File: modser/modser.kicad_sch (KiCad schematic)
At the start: 3 parts, among them IC1 AS5600-ASOT, U1 DRV8313PWPR, U2 XIAO-RP2040-DIP

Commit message: Schematic draft complete!
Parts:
- added C1, C4, C6, C8: 100 nF, symbol Device:C
- added C10, C11: 22 uF, symbol Device:C
- added C2: 100 uF Polarized, symbol Device:C_Polarized
- added C3: 0.47 uF, symbol Device:C
- added C5: 10 nF, symbol Device:C
- added C7: 10 uF, symbol Device:C
- added C9: 100 pF, symbol Device:C
- added J1: Conn_01x03_Socket, symbol Connector:Conn_01x03_Socket
- added L1: 2.2 uH, symbol Device:L
- added R1: 10 kOhm, symbol Device:R
- added R2: 30.9 kOhm, symbol Device:R
- added R3: 62 kOhm, symbol Device:R
- added U3: AP63203WU-7, LIB_AP63203WU-7:AP63203WU7, symbol 2025-08-06_01-37-09:AP63203WU-7
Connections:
- net +3.3V: now reaches IC1.1 (VDD5V)
- net +3.3V: now also IC1.2 (VDD3V3), U1.15 (V3P3), U2.12 (3V3), C10.1, C11.1, C3.2, C6.1, C9.1, L1.2, R1.2, R2.1
- net GND: now reaches IC1.4 (GND)
- net GND: now also IC1.8 (DIR), U1.10 (PGND3), U1.12 (COMPP), U1.13 (COMPN), U1.14 (GND), U1.19 (~{COMPO}), U1.20 (GND__1), U1.21 (NC), U1.28 (GND__2), U1.6 (PGND1), U1.7 (PGND2), U2.13 (GND), C10.2, C11.2, C2.2, C3.1, C4.2, C6.2, C7.2, R3.2, U3.4 (GND)
- net at IC1.6 (SDA): now also U2.5 (GPIO6/SDA)
- net at IC1.7 (SCL): now also U2.6 (GPIO7/SCL)
- net at U2.1 (GPIO26/ADC0/A0): now also U1.27 (IN1)
- net at U2.2 (GPIO27/ADC1/A1): now also U1.25 (IN2)
- net at U2.3 (GPIO28/ADC2/A2): now also U1.23 (IN3)
- net Enable: now reaches U2.4 (GPIO29/ADC3/A3)
- net Enable: now also U1.22 (EN3), U1.24 (EN2), U1.26 (EN1)
- net at U1.1 (CPL): now also C5.1
- net VCC: now reaches U1.11 (VM__1)
- net VCC: now also U1.4 (VM), C1.1, C2.1, C4.1, C7.1, U3.2 (EN), U3.3 (VIN)
- net at U1.18 (~{FAULT}): now also R1.1
- net at U1.2 (CPH): now also C5.2
- net at U1.3 (VCP): now also C1.2
- net at U1.5 (OUT1): now also J1.1 (Pin_1)
- net at U1.8 (OUT2): now also J1.2 (Pin_2)
- net at U1.9 (OUT3): now also J1.3 (Pin_3)
- new net: C8.2, L1.1, U3.5 (SW)
- new net: C8.1, U3.6 (BST)
- new net RegFB: C9.2, R2.2, R3.1, U3.1 (FB)
- no-connect marks 0 -> 11
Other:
- moved on the sheet: IC1, U1, U2

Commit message: Created general outline, speced passives
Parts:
- added J3: Conn_01x02_Socket, Connector_PinHeader_2.54mm:PinHeader_1x02_P2.54mm_Vertical, symbol Connector:Conn_01x02_Socket
- C1, C3, C4, C5, C6, C8, C9: footprint (none) -> Capacitor_SMD:C_0603_1608Metric_Pad1.08x0.95mm_HandSolder
- C10, C11, C7: footprint (none) -> Capacitor_SMD:C_1206_3216Metric
- J1: footprint (none) -> Connector_PinHeader_2.54mm:PinHeader_1x03_P2.54mm_Vertical
- R1, R2, R3: footprint (none) -> Resistor_SMD:R_0603_1608Metric_Pad0.98x0.95mm_HandSolder
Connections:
- net GND: now also J3.2 (Pin_2)
- net VCC: now also J3.1 (Pin_1)
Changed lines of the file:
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@@
 			)
 		)
-		(property "Footprint" ""
+		(property "Footprint" "Resistor_SMD:R_0603_1608Metric_Pad0.98x0.95mm_HandSolder"
 			(at 179.832 134.62 90)
 			(effects
@@
 	)
 	(symbol
+		(lib_id "Connector:Conn_01x02_Socket")
+		(at 214.63 69.85 0)
+		(unit 1)
+		(exclude_from_sim no)
+		(in_bom yes)
+		(on_board yes)
+		(dnp no)
+		(fields_autoplaced yes)
+		(property "Reference" "J3"
+			(at 215.9 69.8499 0)
+			(effects
+				(font
+					(size 1.27 1.27)
+				)
+				(justify left)
+			)
+		)
+		(property "Value" "Conn_01x02_Socket"
+			(at 215.9 72.3899 0)
+			(effects
+				(font
+					(size 1.27 1.27)
+				)
+				(justify left)
+			)
+		)
+		(property "Footprint" "Connector_PinHeader_2.54mm:PinHeader_1x02_P2.54mm_Vertical"
+			(at 214.63 69.85 0)
+			(effects
+				(font
+					(size 1.27 1.27)
+				)
+				(hide yes)
+			)
+		)
+		(property "Datasheet" "~"
+			(at 214.63 69.85 0)
+			(effects
+				(font
+					(size 1.27 1.27)
+				)
+				(hide yes)
+			)
+		)
+		(property "Description" "Generic connector, single row, 01x02, script generated"
+			(at 214.63 69.85 0)
+			(effects
+				(font
+					(size 1.27 1.27)
+				)
+				(hide yes)
+			)
+		)
+		(pin "2"
+		)
+		(pin "1"
+		)
+		(instances
+			(project ""
+				(path "/01c17a33-9bbc-4187-99d4-a03f0d327a97"
+					(reference "J3")
+					(unit 1)
+				)
+			)
+		)
+	)
+	(symbol
 		(lib_id "power:+3.3V")
 		(at 210.82 123.19 270)
@@
 	)
 	(symbol
+		(lib_id "power:GND")
+		(at 209.55 72.39 270)
+		(unit 1)
+		(exclude_from_sim no)
+		(in_bom yes)
+		(on_board yes)
+		(dnp no)
+		(fields_autoplaced yes)
+		(property "Reference" "#PWR014"
+			(at 203.2 72.39 0)
+			(effects
+				(font
+					(size 1.27 1.27)
+				)
+				(hide yes)
+			)
+		)
+		(property "Value" "GND"
+			(at 205.74 72.3899 90)
+			(effects
+				(font
+					(size 1.27 1.27)
+				)
+				(justify right)
+			)
+		)
+		(property "Footprint" ""
+			(at 209.55 72.39 0)
+			(effects
+				(font
+					(size 1.27 1.27)
+				)
+				(hide yes)
+			)
+		)
+		(property "Datasheet" ""
+			(at 209.55 72.39 0)
+			(effects
+				(font
+					(size 1.27 1.27)
+				)
+				(hide yes)
+			)
+		)
+		(property "Description" "Power symbol creates a global label with name \"GND\" , ground"
+			(at 209.55 72.39 0)
+			(effects
+				(font
+					(size 1.27 1.27)
+				)
+				(hide yes)
+			)
+		)
+		(pin "1"
+		)
+		(instances
+			(project "modser"
+				(path "/01c17a33-9bbc-4187-99d4-a03f0d327a97"
+					(reference "#PWR014")
+					(unit 1)
+				)
+			)
+		)
+	)
+	(symbol
 		(lib_id "Device:L")
 		(at 166.37 123.19 90)
@@
 			)
 		)
-		(property "Footprint" ""
+		(property "Footprint" "Capacitor_SMD:C_0603_1608Metric_Pad1.08x0.95mm_HandSolder"
 			(at 159.0548 58.42 0)
 			(effects
@@
 			)
 		)
-		(property "Footprint" ""
+		(property "Footprint" "Capacitor_SMD:C_0603_1608Metric_Pad1.08x0.95mm_HandSolder"
 			(at 161.29 114.6048 0)
 			(effects
@@
 			)
 		)
-		(property "Footprint" ""
+		(property "Footprint" "Resistor_SMD:R_0603_1608Metric_Pad0.98x0.95mm_HandSolder"
 			(at 154.94 60.198 90)
 			(effects
@@
 			)
 		)
-		(property "Footprint" ""
+		(property "Footprint" "Capacitor_SMD:C_0603_1608Metric_Pad1.08x0.95mm_HandSolder"
 			(at 171.1452 130.81 0)
 			(effects
@@
 			)
 		)
-		(property "Footprint" ""
+		(property "Footprint" "Capacitor_SMD:C_0603_1608Metric_Pad1.08x0.95mm_HandSolder"
 			(at 152.0952 45.72 0)
 			(effects
@@
 			)
 		)
-		(property "Footprint" ""
+		(property "Footprint" "Capacitor_SMD:C_1206_3216Metric"
 			(at 200.3552 134.62 0)
 			(effects
@@
 			)
 		)
-		(property "Footprint" ""
+		(property "Footprint" "Capacitor_SMD:C_0603_1608Metric_Pad1.08x0.95mm_HandSolder"
 			(at 40.3352 135.89 0)
 			(effects
@@
 	)
 	(symbol
+		(lib_id "power:VCC")
+		(at 209.55 69.85 90)
+		(unit 1)
+		(exclude_from_sim no)
+		(in_bom yes)
+		(on_board yes)
+		(dnp no)
+		(fields_autoplaced yes)
+		(property "Reference" "#PWR013"
+			(at 213.36 69.85 0)
+			(effects
+				(font
+					(size 1.27 1.27)
+				)
+				(hide yes)
+			)
+		)
+		(property "Value" "VCC"
+			(at 205.74 69.8499 90)
+			(effects
+				(font
+					(size 1.27 1.27)
+				)
+				(justify left)
+			)
+		)
+		(property "Footprint" ""
+			(at 209.55 69.85 0)
+			(effects
+				(font
+					(size 1.27 1.27)
+				)
+				(hide yes)
+			)
+		)
+		(property "Datasheet" ""
+			(at 209.55 69.85 0)
+			(effects
+				(font
+					(size 1.27 1.27)
+				)
+				(hide yes)
+			)
+		)
+		(property "Description" "Power symbol creates a global label with name \"VCC\""
+			(at 209.55 69.85 0)
+			(effects
+				(font
+					(size 1.27 1.27)
+				)
+				(hide yes)
+			)
+		)
+		(pin "1"
+		)
+		(instances
+			(project "modser"
+				(path "/01c17a33-9bbc-4187-99d4-a03f0d327a97"
+					(reference "#PWR013")
+					(unit 1)
+				)
+			)
+		)
+	)
+	(symbol
 		(lib_id "Device:R")
 		(at 181.61 127 0)
@@
 			)
 		)
-		(property "Footprint" ""
+		(property "Footprint" "Resistor_SMD:R_0603_1608Metric_Pad0.98x0.95mm_HandSolder"
 			(at 179.832 127 90)
 			(effects
@@
 			)
 		)
-		(property "Footprint" ""
+		(property "Footprint" "Capacitor_SMD:C_0603_1608Metric_Pad1.08x0.95mm_HandSolder"
 			(at 188.9252 43.18 0)
 			(effects
@@
 			)
 		)
-		(property "Footprint" ""
+		(property "Footprint" "Capacitor_SMD:C_0603_1608Metric_Pad1.08x0.95mm_HandSolder"
 			(at 153.3652 27.94 0)
 			(effects
@@
 			)
 		)
-		(property "Footprint" ""
+		(property "Footprint" "Capacitor_SMD:C_1206_3216Metric"
 			(at 211.7852 134.62 0)
 			(effects
@@
 			)
 		)
-		(property "Footprint" ""
+		(property "Footprint" "Capacitor_SMD:C_1206_3216Metric"
 			(at 113.9952 137.16 0)
 			(effects
@@
 			)
 		)
-		(property "Footprint" ""
+		(property "Footprint" "Connector_PinHeader_2.54mm:PinHeader_1x03_P2.54mm_Vertical"
 			(at 196.85 50.8 0)
 			(effects

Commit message: Finished layout, working on getting all 3d models added
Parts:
- C2: footprint (none) -> LIB_UCL1E101MCL1GS:CAPAE660X800N
- L1: footprint (none) -> LQM2MPN2R2NG0L:INDC2016X100N
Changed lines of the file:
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@@
 			)
 		)
-		(property "Footprint" ""
+		(property "Footprint" "LQM2MPN2R2NG0L:INDC2016X100N"
 			(at 166.37 123.19 0)
 			(effects
@@
 			)
 		)
-		(property "Footprint" ""
+		(property "Footprint" "LIB_UCL1E101MCL1GS:CAPAE660X800N"
 			(at 166.0652 43.18 0)
 			(effects

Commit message: Fixed issue with design around power regulator
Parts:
- removed C9: 100 pF, Capacitor_SMD:C_0603_1608Metric_Pad1.08x0.95mm_HandSolder, symbol Device:C
- removed R2: 30.9 kOhm, Resistor_SMD:R_0603_1608Metric_Pad0.98x0.95mm_HandSolder, symbol Device:R
- removed R3: 62 kOhm, Resistor_SMD:R_0603_1608Metric_Pad0.98x0.95mm_HandSolder, symbol Device:R
- L1: value 2.2 uH -> 3.9 uH
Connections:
- net RegFB is gone; now on net +3.3V: U3.1 (FB)

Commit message: Fixed issue where reset and sleep lines were never pulled high as required
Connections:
- net Enable: now also U1.16 (~{RESET}), U1.17 (~{SLEEP})
- no-connect marks 11 -> 9
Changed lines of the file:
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@@
+	)
+	(junction
+		(at 107.95 43.18)
+		(diameter 0)
+		(color 0 0 0 0)
 	)
 	(junction
@@
 	)
 	(junction
+		(at 107.95 38.1)
+		(diameter 0)
+		(color 0 0 0 0)
+	)
+	(junction
 		(at 199.39 138.43)
 		(diameter 0)
@@
 		(diameter 0)
 		(color 0 0 0 0)
-	)
-	(no_connect
-		(at 111.76 35.56)
 	)
 	(no_connect
@@
 	)
 	(no_connect
-		(at 111.76 38.1)
-	)
-	(no_connect
 		(at 80.01 97.79)
 	)
@@
 	(wire
 		(pts
+			(xy 107.95 43.18) (xy 107.95 38.1)
+		)
+		(stroke
+			(width 0)
+			(type default)
+		)
+	)
+	(wire
+		(pts
 			(xy 147.32 81.28) (xy 165.1 81.28)
 		)
@@
 	(wire
 		(pts
+			(xy 107.95 38.1) (xy 107.95 35.56)
+		)
+		(stroke
+			(width 0)
+			(type default)
+		)
+	)
+	(wire
+		(pts
 			(xy 39.37 90.17) (xy 44.45 90.17)
 		)
@@
 	(wire
 		(pts
+			(xy 107.95 35.56) (xy 111.76 35.56)
+		)
+		(stroke
+			(width 0)
+			(type default)
+		)
+	)
+	(wire
+		(pts
 			(xy 165.1 43.18) (xy 165.1 66.04)
 		)
@@
 		)
 		(stroke
+			(width 0)
+			(type default)
+		)
+	)
+	(wire
+		(pts
+			(xy 107.95 38.1) (xy 111.76 38.1)
+		)
+		(stroke

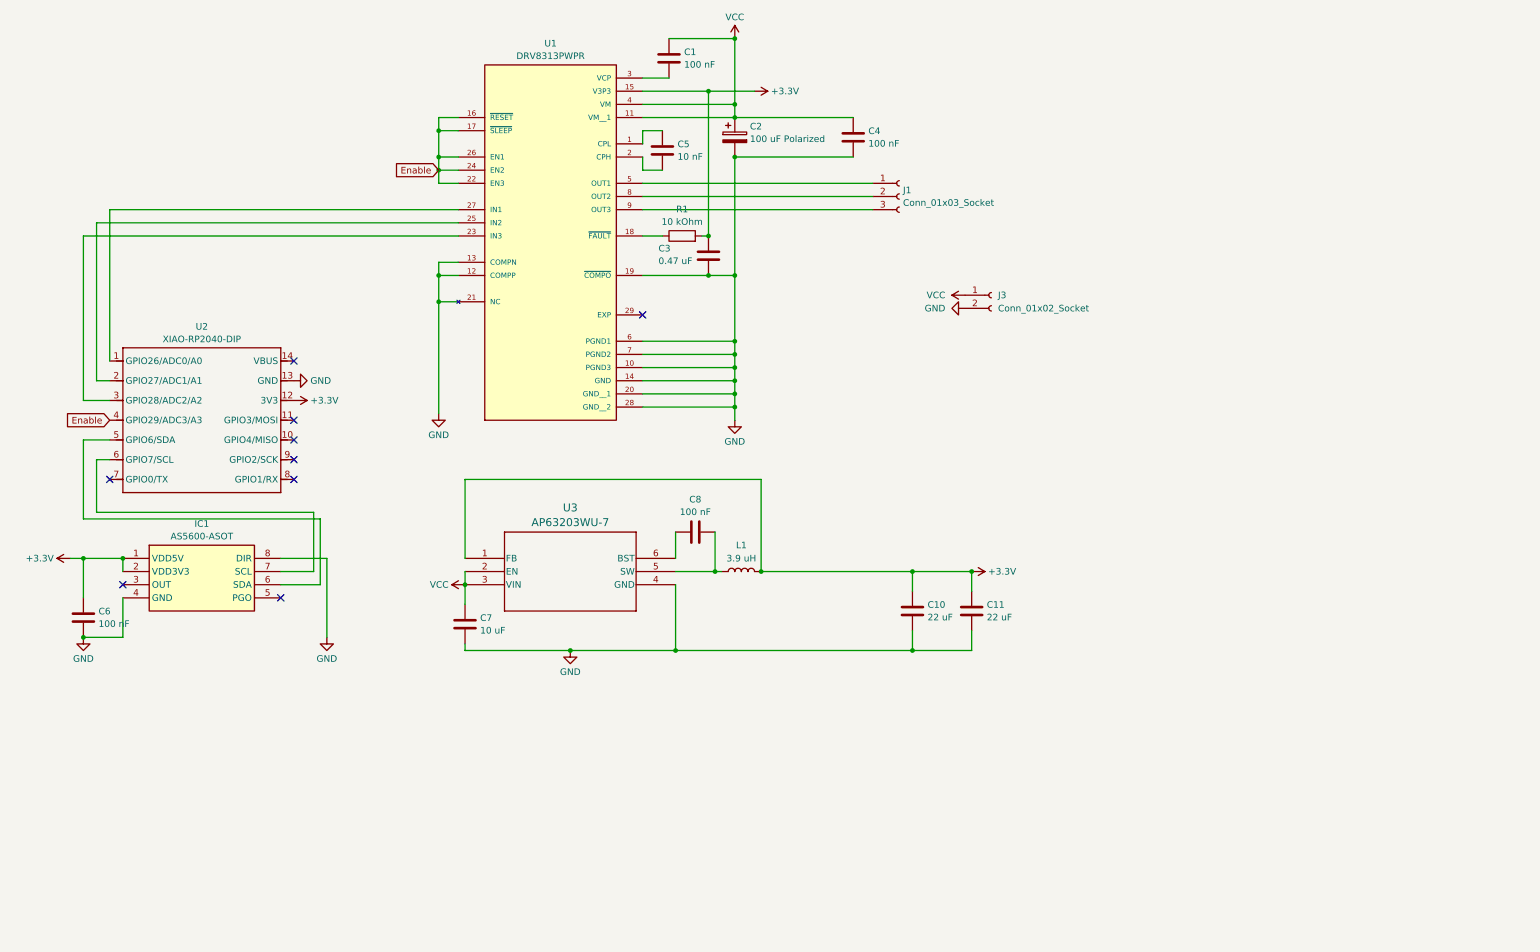
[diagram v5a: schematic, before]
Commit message: Updated schematic with can bus lines
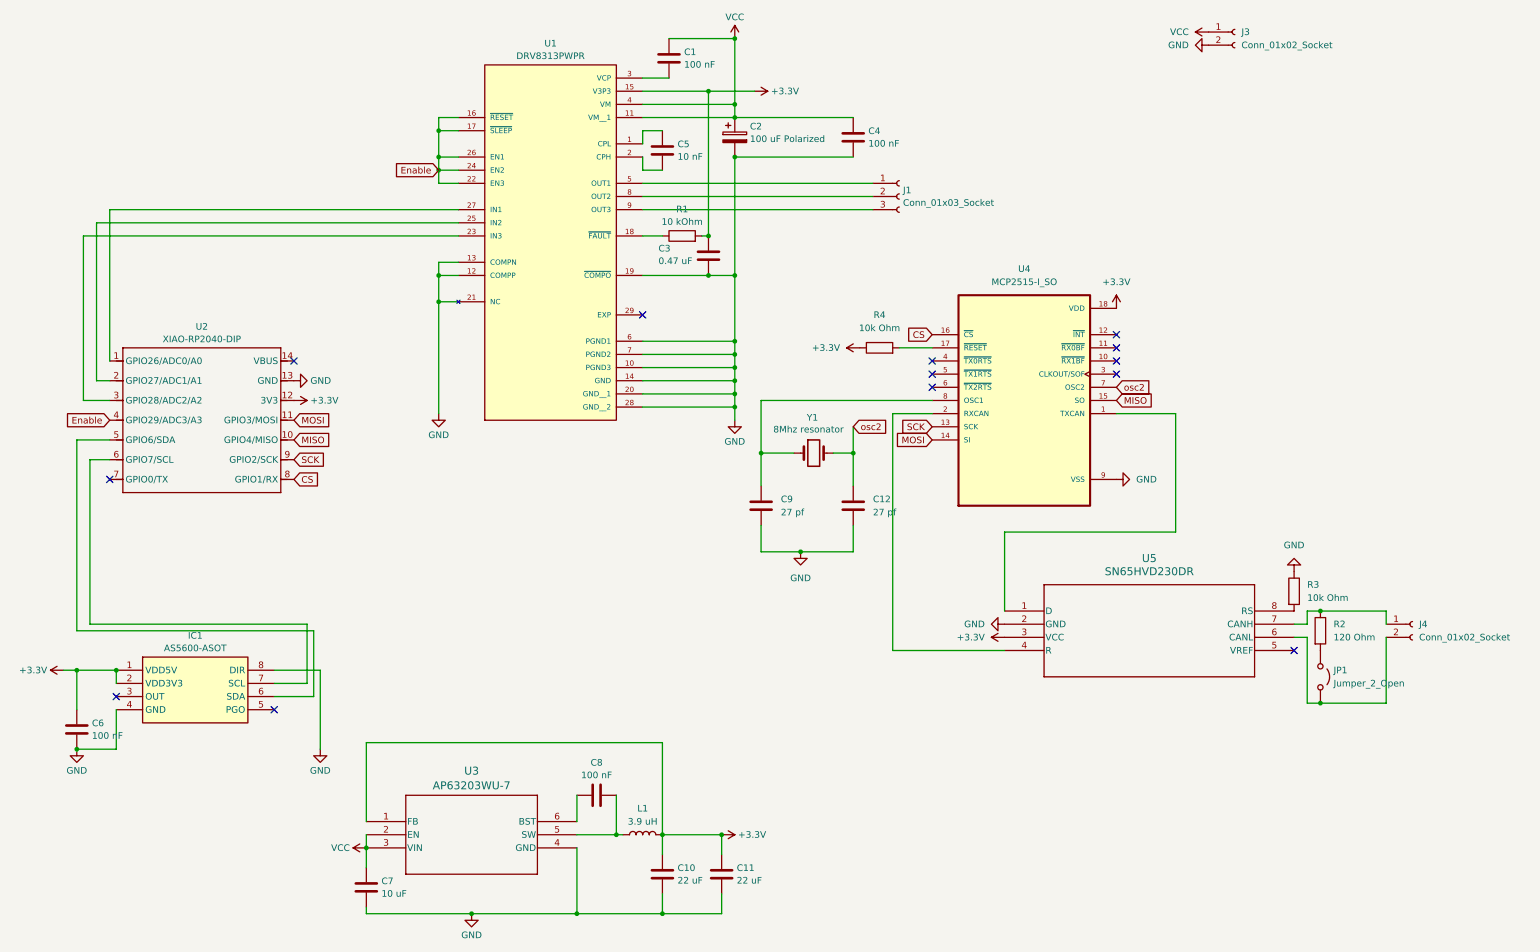
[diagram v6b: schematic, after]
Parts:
- added C12, C9: 27 pf, symbol Device:C
- added J4: Conn_01x02_Socket, symbol Connector:Conn_01x02_Socket
- added JP1: Jumper_2_Open, symbol Jumper:Jumper_2_Open
- added R2: 120 Ohm, symbol Device:R
- added R3, R4: 10k Ohm, symbol Device:R
- added U4: MCP2515-I_SO, MCP2515-I_SO:SOIC127P1030X265-18N, symbol MCP2515-I_SO:MCP2515-I_SO
- added U5: SN65HVD230DR, D8, symbol 2025-11-09_01-42-57:SN65HVD230DR
- added Y1: 8Mhz resonator, symbol Device:Crystal
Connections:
- net +3.3V: now also R4.1, U4.18 (VDD), U5.3 (VCC)
- net GND: now also C12.2, C9.2, R3.1, U4.9 (VSS), U5.2 (GND)
- net MISO: now reaches U2.10 (GPIO4/MISO)
- net MISO: now also U4.15 (SO)
- net MOSI: now reaches U2.11 (GPIO3/MOSI)
- net MOSI: now also U4.14 (SI)
- net CS: now reaches U2.8 (GPIO1/RX)
- net CS: now also U4.16 (~{CS})
- net SCK: now reaches U2.9 (GPIO2/SCK)
- net SCK: now also U4.13 (SCK)
- new net: J4.1 (Pin_1), R2.1, U5.7 (CANH)
- new net: JP1.1 (A), R2.2
- new net: R4.2, U4.17 (~{RESET})
- new net: C9.1, U4.8 (OSC1), Y1.1
- new net: J4.2 (Pin_2), JP1.2 (B), U5.6 (CANL)
- new net: U4.1 (TXCAN), U5.1 (D)
- new net: U4.2 (RXCAN), U5.4 (R)
- new net: R3.2, U5.8 (RS)
- new net osc2: C12.1, U4.7 (OSC2), Y1.2
- no-connect marks 9 -> 13
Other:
- moved on the sheet: C10, C11, C6, C7, C8, IC1, J3, L1, U3

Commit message: Sent for production
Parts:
- C12, C9: value 27 pf -> 22 pf; footprint (none) -> Capacitor_SMD:C_0603_1608Metric_Pad1.08x0.95mm_HandSolder
- J4: footprint (none) -> Connector_PinHeader_2.54mm:PinHeader_1x02_P2.54mm_Vertical
- JP1: footprint (none) -> Jumper:SolderJumper-2_P1.3mm_Bridged_RoundedPad1.0x1.5mm
- R2, R3, R4: footprint (none) -> Resistor_SMD:R_0603_1608Metric_Pad0.98x0.95mm_HandSolder
- U4: footprint MCP2515-I_SO:SOIC127P1030X265-18N -> MCP2515_I_SO:SOIC127P1030X265-18N
- Y1: footprint (none) -> NX3225GD_8MHZ_STD_CRA_3:XTAL_NX3225GD-8MHZ-STD-CRA-3_NDK
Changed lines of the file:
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@@
 			)
 		)
-		(property "Footprint" ""
+		(property "Footprint" "Resistor_SMD:R_0603_1608Metric_Pad0.98x0.95mm_HandSolder"
 			(at 276.352 134.62 90)
 			(effects
@@
 			)
 		)
-		(property "Footprint" ""
+		(property "Footprint" "Resistor_SMD:R_0603_1608Metric_Pad0.98x0.95mm_HandSolder"
 			(at 193.04 81.788 90)
 			(effects
@@
 			)
 		)
-		(property "Footprint" ""
+		(property "Footprint" "NX3225GD_8MHZ_STD_CRA_3:XTAL_NX3225GD-8MHZ-STD-CRA-3_NDK"
 			(at 180.34 100.33 0)
 			(effects
@@
 			)
 		)
-		(property "Footprint" ""
+		(property "Footprint" "Connector_PinHeader_2.54mm:PinHeader_1x02_P2.54mm_Vertical"
 			(at 295.91 133.35 0)
 			(effects
@@
 			)
 		)
-		(property "Footprint" ""
+		(property "Footprint" "Jumper:SolderJumper-2_P1.3mm_Bridged_RoundedPad1.0x1.5mm"
 			(at 278.13 143.51 0)
 			(effects
@@
 			)
 		)
-		(property "Value" "27 pf"
+		(property "Value" "22 pf"
 			(at 191.77 111.7599 0)
 			(effects
@@
 			)
 		)
-		(property "Footprint" ""
+		(property "Footprint" "Capacitor_SMD:C_0603_1608Metric_Pad1.08x0.95mm_HandSolder"
 			(at 188.9252 114.3 0)
 			(effects
@@
 			)
 		)
-		(property "Footprint" "MCP2515-I_SO:SOIC127P1030X265-18N"
+		(property "Footprint" "MCP2515_I_SO:SOIC127P1030X265-18N"
 			(at 220.98 90.17 0)
 			(effects
@@
 			)
 		)
-		(property "Value" "27 pf"
+		(property "Value" "22 pf"
 			(at 173.99 111.7599 0)
 			(effects
@@
 			)
 		)
-		(property "Footprint" ""
+		(property "Footprint" "Capacitor_SMD:C_0603_1608Metric_Pad1.08x0.95mm_HandSolder"
 			(at 171.1452 114.3 0)
 			(effects
@@
 			)
 		)
-		(property "Footprint" ""
+		(property "Footprint" "Resistor_SMD:R_0603_1608Metric_Pad0.98x0.95mm_HandSolder"
 			(at 271.272 127 90)
 			(effects
